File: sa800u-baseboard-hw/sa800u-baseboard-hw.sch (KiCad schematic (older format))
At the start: 23 parts, among them IC1 TPS2378DDA

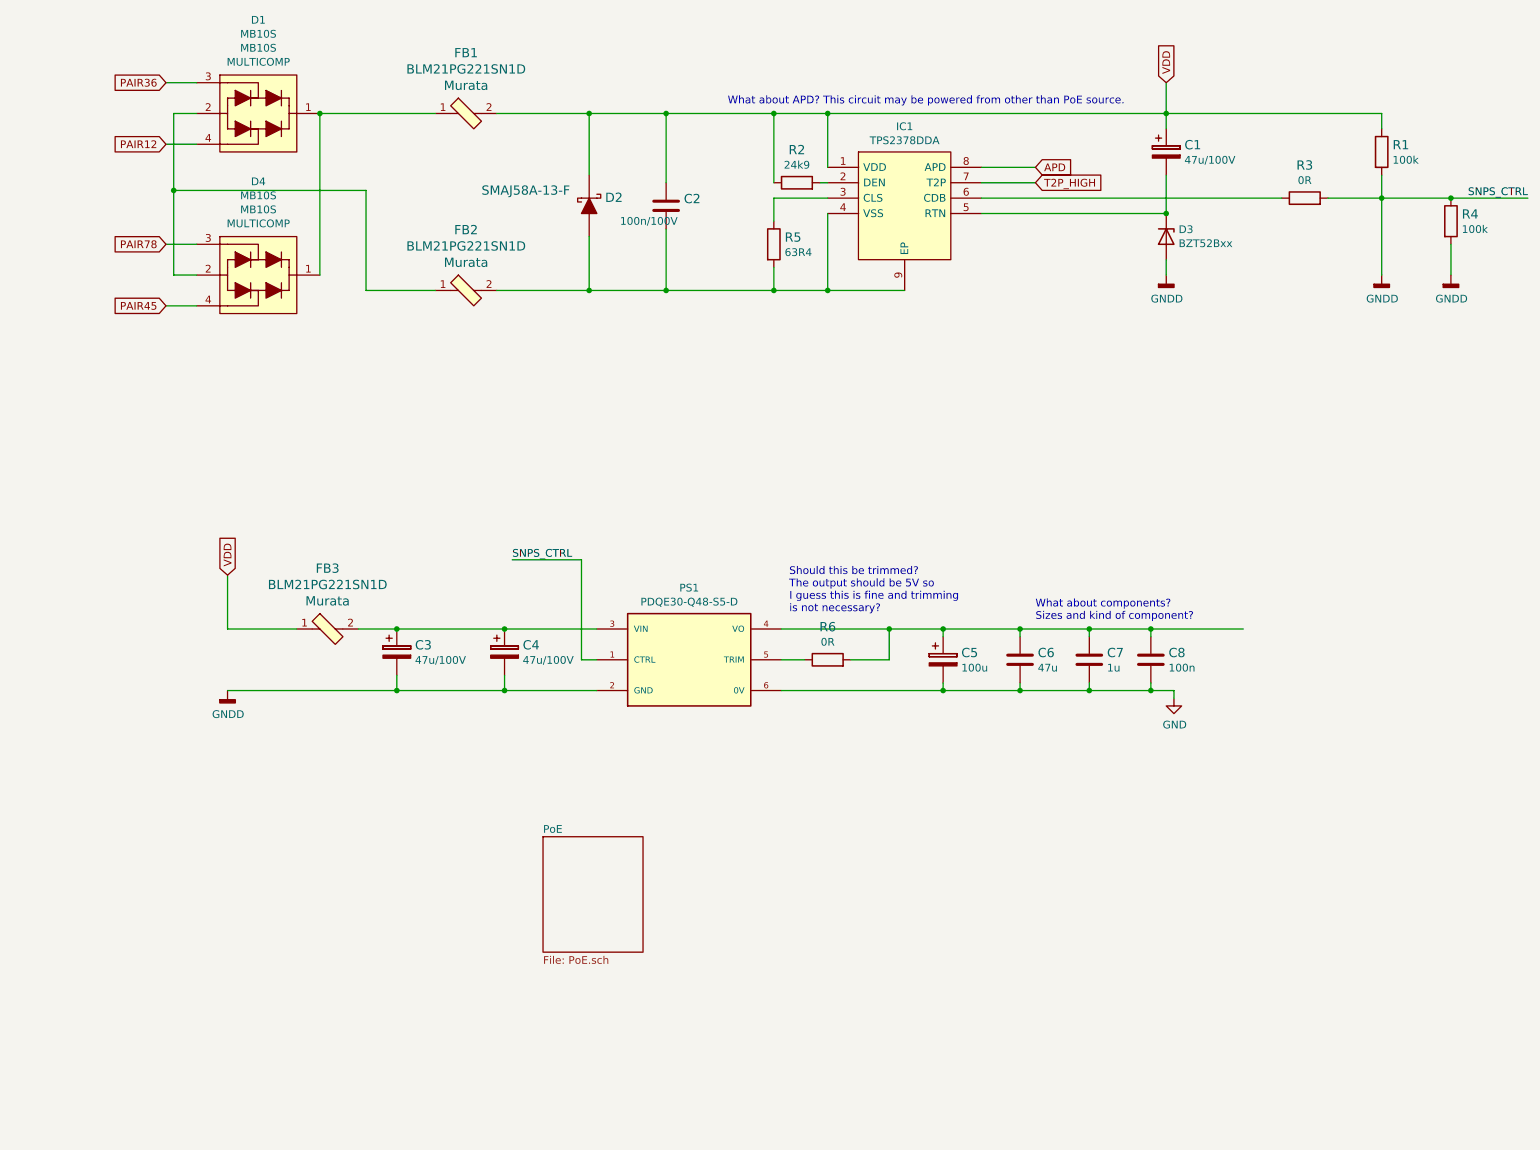
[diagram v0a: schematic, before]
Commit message: added initial version of ethernet controller
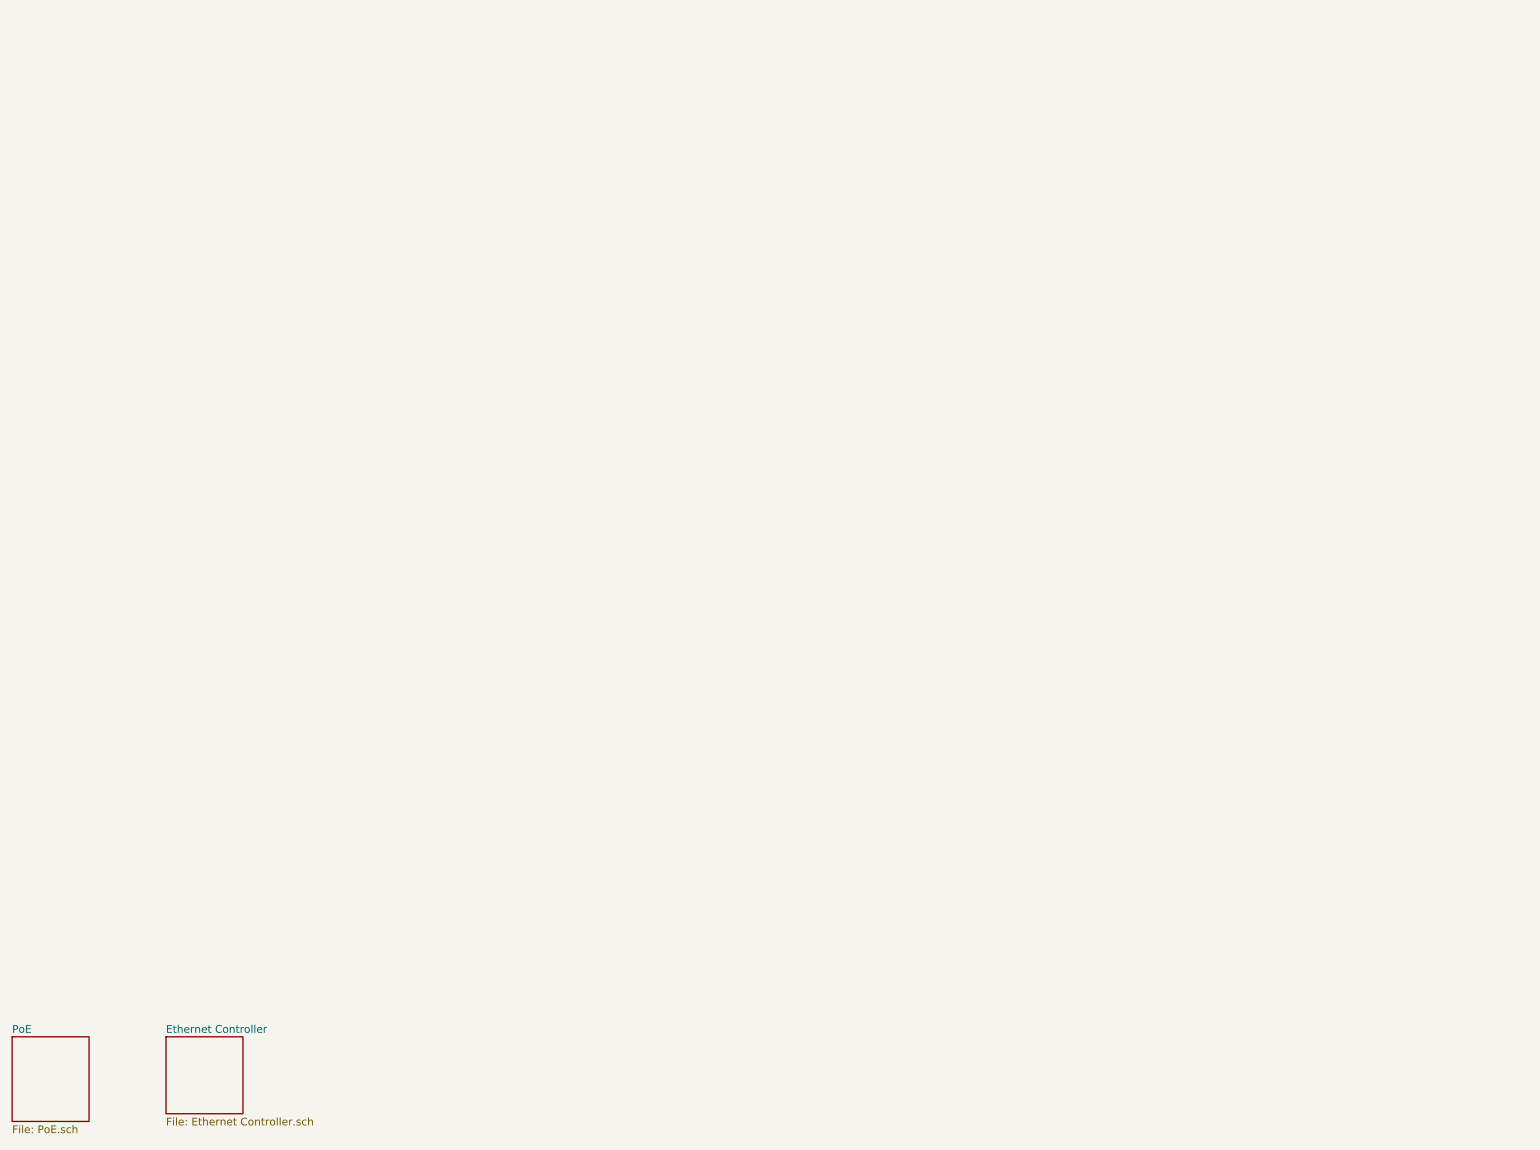
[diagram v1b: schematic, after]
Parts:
- removed C1, C3, C4: C_47u_ELEC_100V, antmicro-footprints:CP_Elec_10x10.5, symbol antmicroCapacitorspol:C_47u_ELEC_100V
- removed C2: C_100n_0805_100V, antmicro-footprints:0805-cap, symbol antmicroCapacitorsmisc:C_100n_0805_100V
- removed C5: C_100u_KEMET_A, antmicro-footprints:KEMET_A, symbol antmicroCapacitorspol:C_100u_KEMET_A
- removed C6: C_47u_0805, antmicro-footprints:0805-cap, symbol antmicroCapacitorsmisc:C_47u_0805
- removed C7: C_1u_0402, antmicro-footprints:0402-cap, symbol antmicroCapacitors0402:C_1u_0402
- removed C8: C_100n_0402, antmicro-footprints:0402-cap, symbol antmicroCapacitors0402:C_100n_0402
- removed D1, D4: MB10S, antmicro-footprints:MB10S, symbol antmicroTVSDiodes:MB10S
- removed D2: SMAJ58A-13-F, antmicro-footprints:DO-214AC, symbol antmicroDiodesRectifiersSingle:SMAJ58A-13-F
- removed D3: BZT52Bxx, antmicro-footprints:SOD-123, symbol antmicroDiodesZenerSingle:BZT52Bxx
- removed FB1, FB2, FB3: BLM21PG221SN1D, antmicro-footprints:0805-res, symbol antmicroFerriteBeadsandChips:BLM21PG221SN1D
- removed IC1: TPS2378DDA, antmicro-footprints:SOIC127P600X170-9N, symbol antmicroPMICPowerDistributionSwitchesLoadDrivers:TPS2378DDA
- removed PS1: PDQE30-Q48-S5-D, antmicro-footprints:PDQE30-Q48, symbol antmicroDCDCConverters:PDQE30-Q48-S5-D
- removed R1, R4: R_100k_0402, antmicro-footprints:0402-res, symbol antmicroResistors0402:R_100k_0402
- removed R2: R_24k9_0402, antmicro-footprints:0402-res, symbol antmicroResistors0402:R_24k9_0402
- removed R3, R6: R_0R_0402, antmicro-footprints:0402-res, symbol antmicroResistors0402:R_0R_0402
- removed R5: R_63R4_0402, antmicro-footprints:0402-res, symbol antmicroResistors0402:R_63R4_0402
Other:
- note removed: "Should this be trimmed? \nThe output should be 5V so\nI guess this is fine and trimming\nis not necessary?"
- note removed: "What about APD? This circuit may be powered from other than PoE source."
- note removed: "What about components? \nSizes and kind of component?"

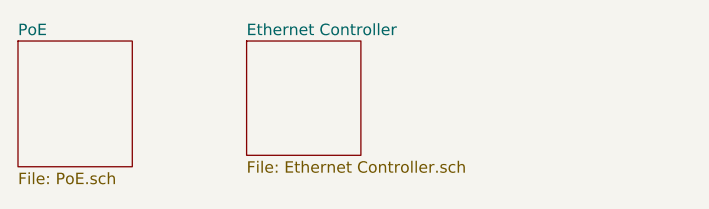
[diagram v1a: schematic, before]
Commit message: added ethernet oscillator and some controll pins
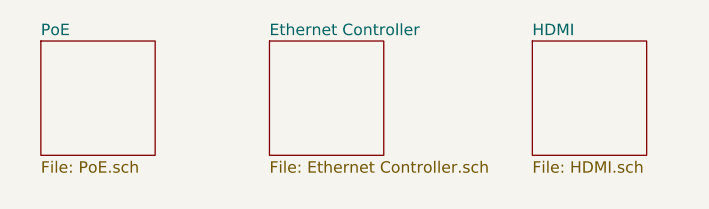
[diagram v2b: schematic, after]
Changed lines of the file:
@@
 $Descr A4 11693 8268
 encoding utf-8
-Sheet 1 3
+Sheet 1 4
 Title ""
 Date ""
@@
 $EndDescr
 $Sheet
-S 500  7000 500  550
+S 600  7000 500  500
 U 61A19323
 F0 "PoE" 50
@@
 $EndSheet
 $Sheet
-S 1500 7000 500  500
+S 1600 7000 500  500
 U 618E716E
 F0 "Ethernet Controller" 50
 F1 "Ethernet Controller.sch" 50
 $EndSheet
+$Sheet
+S 2750 7000 500  500
+U 6197686D
+F0 "HDMI" 50
+F1 "HDMI.sch" 50
+$EndSheet
 $EndSCHEMATC
